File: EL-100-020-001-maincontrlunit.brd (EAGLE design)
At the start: 68 x 86 mm, 13 parts, among them T1 WS-TST-90°, U19 ABS10-32.768KHZ-7-T, U8 MCP7940N-I/SN, U9 PMEG2005ET, X1 944-12-46-00, X2 944-12-46-00

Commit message: update layout
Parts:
- moved X2 0.40 mm to (52.2, 18.5)
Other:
- board size 68 x 86 mm -> 68 x 87 mm
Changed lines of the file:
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@@
 <setting verticaltext="up"/>
 </settings>
-<grid distance="1" unitdist="mm" unit="mm" style="lines" multiple="1" display="no" altdistance="0.025" altunitdist="inch" altunit="inch"/>
+<grid distance="0.1" unitdist="mm" unit="mm" style="lines" multiple="1" display="no" altdistance="0.025" altunitdist="inch" altunit="inch"/>
 <layers>
 <layer number="1" name="Top" color="4" fill="1" visible="yes" active="yes"/>
-<layer number="2" name="Route2" color="1" fill="3" visible="no" active="yes"/>
+<layer number="2" name="Route2" color="1" fill="3" visible="yes" active="yes"/>
 <layer number="3" name="Route3" color="4" fill="3" visible="no" active="no"/>
 <layer number="14" name="Route14" color="1" fill="6" visible="no" active="no"/>
-<layer number="15" name="Route15" color="4" fill="6" visible="no" active="yes"/>
+<layer number="15" name="Route15" color="4" fill="6" visible="yes" active="yes"/>
 <layer number="16" name="Bottom" color="1" fill="1" visible="yes" active="yes"/>
 <layer number="17" name="Pads" color="2" fill="1" visible="yes" active="yes"/>
@@
 <layer number="45" name="Holes" color="7" fill="1" visible="no" active="yes"/>
 <layer number="46" name="Milling" color="3" fill="1" visible="no" active="yes"/>
-<layer number="47" name="Measures" color="7" fill="1" visible="no" active="yes"/>
+<layer number="47" name="Measures" color="7" fill="1" visible="yes" active="yes"/>
 <layer number="48" name="Document" color="7" fill="1" visible="yes" active="yes"/>
 <layer number="49" name="Reference" color="7" fill="1" visible="yes" active="yes"/>
@@
 <plain>
 <wire x1="0" y1="0" x2="68" y2="0" width="0" layer="20"/>
-<wire x1="68" y1="0" x2="68" y2="86" width="0" layer="20"/>
-<wire x1="68" y1="86" x2="0" y2="86" width="0" layer="20"/>
-<wire x1="0" y1="86" x2="0" y2="0" width="0" layer="20"/>
+<wire x1="68" y1="0" x2="68" y2="87" width="0" layer="20"/>
+<wire x1="68" y1="87" x2="0" y2="87" width="0" layer="20"/>
+<wire x1="0" y1="87" x2="0" y2="0" width="0" layer="20"/>
+<dimension x1="3.9" y1="18.54" x2="52.2" y2="18.54" x3="28.05" y3="11" textsize="1.778" layer="47"/>
+<dimension x1="56" y1="52.8" x2="68" y2="52.8" x3="62" y3="49.6" textsize="1.778" layer="47"/>
 </plain>
 <attributes>
@@
 <attribute name="OC_FARNELL" value="unknown" x="3.9" y="18.54" size="1.778" layer="27" rot="R90" display="off"/>
 </element>
-<element name="X2" library="strasys_standard" package="2,54_STIFTLEIST_2X23" value="944-12-46-00" x="52.6" y="18.54" rot="R90">
-<attribute name="MPN" value="" x="52.6" y="18.54" size="1.778" layer="27" rot="R90" display="off"/>
-<attribute name="SUPPLIER" value="W+P" x="52.6" y="18.54" size="1.778" layer="27" rot="R90" display="off"/>
-<attribute name="MF" value="" x="52.6" y="18.54" size="1.778" layer="27" rot="R90" display="off"/>
-<attribute name="OC_FARNELL" value="unknown" x="52.6" y="18.54" size="1.778" layer="27" rot="R90" display="off"/>
+<element name="X2" library="strasys_standard" package="2,54_STIFTLEIST_2X23" value="944-12-46-00" x="52.2" y="18.54" rot="R90">
+<attribute name="MPN" value="" x="52.2" y="18.54" size="1.778" layer="27" rot="R90" display="off"/>
+<attribute name="SUPPLIER" value="W+P" x="52.2" y="18.54" size="1.778" layer="27" rot="R90" display="off"/>
+<attribute name="MF" value="" x="52.2" y="18.54" size="1.778" layer="27" rot="R90" display="off"/>
+<attribute name="OC_FARNELL" value="unknown" x="52.2" y="18.54" size="1.778" layer="27" rot="R90" display="off"/>
 </element>
 </elements>
@@
 <contactref element="X2" pad="P3"/>
 <contactref element="X2" pad="P4"/>
-<wire x1="52.6" y1="21.08" x2="24.8138" y2="59.235" width="0" layer="19" extent="1-1"/>
-<wire x1="55.14" y1="21.08" x2="52.6" y2="21.08" width="0" layer="19" extent="1-1"/>
-<wire x1="37.4782" y1="37.74" x2="52.6" y2="21.08" width="0" layer="19" extent="1-1"/>
+<wire x1="52.2" y1="21.08" x2="24.8138" y2="59.235" width="0" layer="19" extent="1-1"/>
+<wire x1="54.74" y1="21.08" x2="52.2" y2="21.08" width="0" layer="19" extent="1-1"/>
+<wire x1="37.4782" y1="37.74" x2="52.2" y2="21.08" width="0" layer="19" extent="1-1"/>
 <wire x1="24.9512" y1="19.96" x2="37.4782" y2="37.74" width="0" layer="19" extent="1-1"/>
 </signal>
@@
 <contactref element="X2" pad="P44"/>
 <contactref element="X2" pad="P46"/>
-<wire x1="55.14" y1="74.42" x2="36.43" y2="78.84" width="0" layer="19" extent="1-1"/>
-<wire x1="52.6" y1="74.42" x2="55.14" y2="74.42" width="0" layer="19" extent="1-1"/>
-<wire x1="55.14" y1="71.88" x2="55.14" y2="74.42" width="0" layer="19" extent="1-1"/>
-<wire x1="52.6" y1="71.88" x2="52.6" y2="74.42" width="0" layer="19" extent="1-1"/>
-<wire x1="19.8862" y1="55.425" x2="52.6" y2="71.88" width="0" layer="19" extent="1-1"/>
+<wire x1="54.74" y1="74.42" x2="36.43" y2="78.84" width="0" layer="19" extent="1-1"/>
+<wire x1="52.2" y1="74.42" x2="54.74" y2="74.42" width="0" layer="19" extent="1-1"/>
+<wire x1="54.74" y1="71.88" x2="54.74" y2="74.42" width="0" layer="19" extent="1-1"/>
+<wire x1="52.2" y1="71.88" x2="52.2" y2="74.42" width="0" layer="19" extent="1-1"/>
+<wire x1="19.8862" y1="55.425" x2="52.2" y2="71.88" width="0" layer="19" extent="1-1"/>
 <wire x1="6.44" y1="18.54" x2="19.8862" y2="55.425" width="0" layer="19" extent="1-1"/>
 <wire x1="3.9" y1="18.54" x2="6.44" y2="18.54" width="0" layer="19" extent="1-1"/>
-<wire x1="52.6" y1="18.54" x2="6.44" y2="18.54" width="0" layer="19" extent="1-1"/>
-<wire x1="55.14" y1="18.54" x2="52.6" y2="18.54" width="0" layer="19" extent="1-1"/>
-<wire x1="54.56" y1="3.57" x2="55.14" y2="18.54" width="0" layer="19" extent="1-1"/>
+<wire x1="52.2" y1="18.54" x2="6.44" y2="18.54" width="0" layer="19" extent="1-1"/>
+<wire x1="54.74" y1="18.54" x2="52.2" y2="18.54" width="0" layer="19" extent="1-1"/>
+<wire x1="54.56" y1="3.57" x2="54.74" y2="18.54" width="0" layer="19" extent="1-1"/>
 <wire x1="28.3888" y1="28.85" x2="54.56" y2="3.57" width="0" layer="19" extent="1-1"/>
 <wire x1="40.8488" y1="20.96" x2="28.3888" y2="28.85" width="0" layer="19" extent="1-1"/>
@@
 <contactref element="U8" pad="5"/>
 <contactref element="X2" pad="P18"/>
-<wire x1="24.8138" y1="55.425" x2="55.14" y2="38.86" width="0" layer="19" extent="1-1"/>
+<wire x1="24.8138" y1="55.425" x2="54.74" y2="38.86" width="0" layer="19" extent="1-1"/>
 </signal>
 <signal name="I2C1_SCL">
 <contactref element="U8" pad="6"/>
 <contactref element="X2" pad="P17"/>
-<wire x1="24.8138" y1="56.695" x2="52.6" y2="38.86" width="0" layer="19" extent="1-1"/>
+<wire x1="24.8138" y1="56.695" x2="52.2" y2="38.86" width="0" layer="19" extent="1-1"/>
 </signal>
 <signal name="SYS_RESET">
 <contactref element="T1" pad="2"/>
 <contactref element="X2" pad="P10"/>
-<wire x1="50.06" y1="3.57" x2="55.14" y2="28.7" width="0" layer="19" extent="1-1"/>
+<wire x1="50.06" y1="3.57" x2="54.74" y2="28.7" width="0" layer="19" extent="1-1"/>
 </signal>
 <signal name="PE">
@@
 <contactref element="X2" pad="P6"/>
 <contactref element="X2" pad="P5"/>
-<wire x1="52.6" y1="23.62" x2="55.14" y2="23.62" width="0" layer="19" extent="1-1"/>
+<wire x1="52.2" y1="23.62" x2="54.74" y2="23.62" width="0" layer="19" extent="1-1"/>
 </signal>
 <signal name="SYS5V">
 <contactref element="X2" pad="P7"/>
 <contactref element="X2" pad="P8"/>
-<wire x1="52.6" y1="26.16" x2="55.14" y2="26.16" width="0" layer="19" extent="1-1"/>
+<wire x1="52.2" y1="26.16" x2="54.74" y2="26.16" width="0" layer="19" extent="1-1"/>
 </signal>
 <signal name="PWR_BUT">

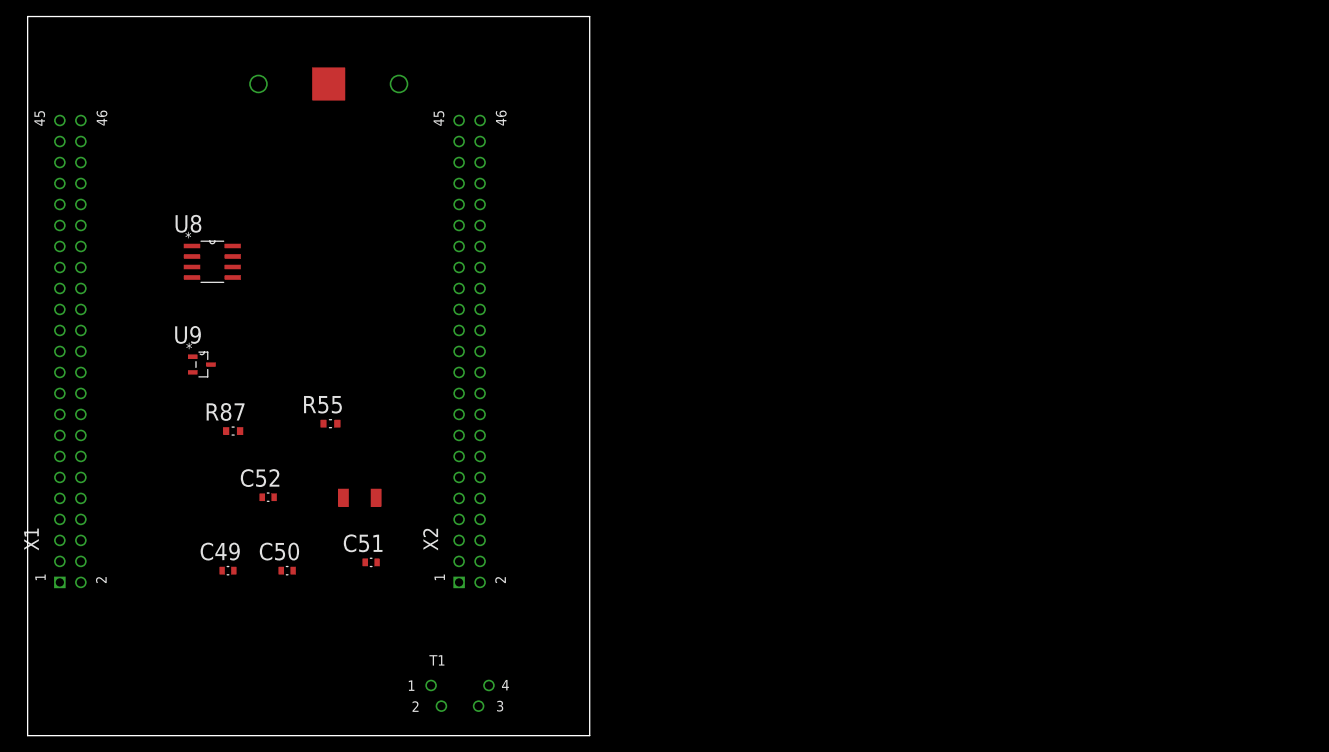
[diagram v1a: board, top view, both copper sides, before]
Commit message: change to size 9
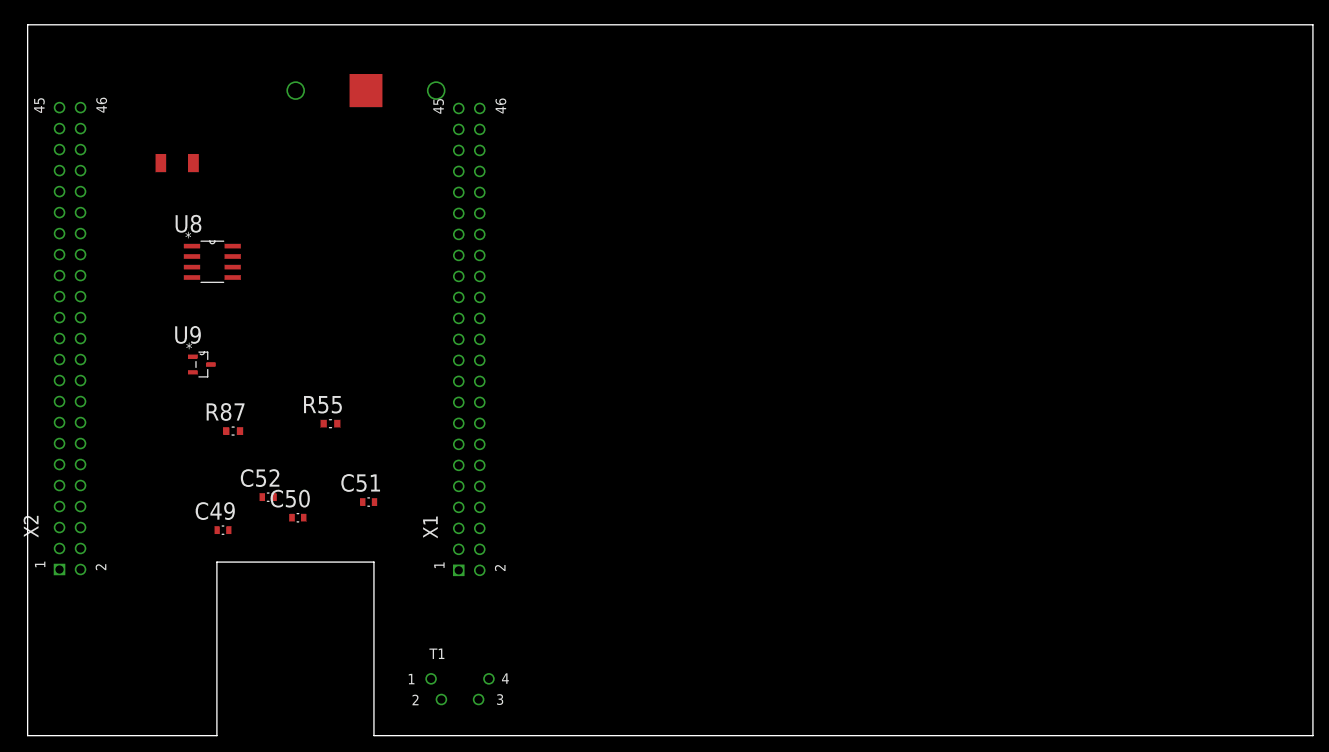
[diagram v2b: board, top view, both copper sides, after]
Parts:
- moved X2 48.4 mm to (3.86, 20.1)
- moved X1 48.3 mm to (52.2, 20.0)
- moved U19 46.1 mm to (18.1, 69.3)
- moved C51 7.31 mm to (41.3, 28.3)
- moved C50 6.53 mm to (32.7, 26.4)
- moved C49 4.94 mm to (23.6, 24.9)
- moved BAT1 4.57 mm to (40.9, 78.0)
- moved T1 0.80 mm to (48.8, 6.87)
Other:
- board size 68 x 87 mm -> 155.5 x 86 mm

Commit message: DIN - Rail
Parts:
- removed R55: 10K Ohms, Vishay_By_element14_Batch_1:RESC1608X60N
- added C1: 47µF, strasys_standard:CAPAE830X650N
- added C10, C3, C4, C5, C6, C7, C8, C9: 10nF, Kemet_By_element14_1:CAPC2013X88N
- added C2, C48: 100nF, Kemet_By_element14_1:CAPC2013X110N
- added D5: SM15T39A, strasys_standard:SM15T39A
- added OC1, OC2, OC3, OC4, OC5, OC6, OC7, OC8: TCMT1106, strasys_standard:SOP-4
- added R1, R2, R3, R4, R5, R6, R7, R8: 1K Ohms, Vishay_By_element14_Batch_1:RESC2013X65N
- added R10, R11, R12, R13, R14, R15, R16, R17: 47K Ohms, Vishay_By_element14_Batch_1:RESC2013X65N
- added R83, R84: 10K Ohms, Vishay_By_element14_Batch_1:RESC2013X65N
- added S1: (no value), switch-dil:SD4-01
- added U1, U2: VNI4140K-32, strasys_standard:SOP80P1030X247-25N
- added U16: 24AA256-I/SN, Microchip_By_element14_Batch_1:SOIC127P600X175-8N
- added X3: 90G-14, strasys_standard:90G-14
- C49: value 0.1uF -> 100nF; device Kemet_By_element14_Batch_1:CAPC1608X85N -> Kemet_By_element14_1:CAPC2013X110N
- C50, C51, C52: device Kemet_By_element14_Batch_1:CAPC1608X85N -> Kemet_By_element14_1:CAPC2013X88N
- R87: device Vishay_By_element14_Batch_1:RESC1608X60N -> Vishay_By_element14_Batch_1:RESC2013X65N
- moved X2 58.5 mm to (62.3, 19.7)
- moved T1 46.3 mm to (2.54, 7.62)
- moved C49 39.3 mm to (41.9, 59.7), turned to 180 degrees
- moved X1 38.1 mm to (14.1, 19.7)
- moved U9 33.8 mm to (50.8, 61.0), turned to 270 degrees
- moved U19 33.6 mm to (43.2, 47.0)
- moved C52 32.9 mm to (49.5, 54.6), turned to 180 degrees
- moved R87 31.9 mm to (49.5, 57.1)
- moved C50 26.6 mm to (45.7, 49.5), turned to 180 degrees
- moved C51 21.3 mm to (40.6, 49.5)
- moved U8 21.0 mm to (43.2, 54.6), turned to 90 degrees
- moved BAT1 6.09 mm to (47.0, 77.5)
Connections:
- net N$35 renamed BAT-SUPPLY
- new net +24V: C1.1, C2.2, D5.K, OC1.4, OC2.4, OC3.4, OC4.4, OC5.4, OC6.4, OC7.4, OC8.4, U1.1, U1.25, U2.1, U2.25
- new net 0V: C1.2, C10.1, C2.1, C3.1, C4.1, C5.1, C6.1, C7.1, C8.1, C9.1, D5.A, R10.2, R11.2, R12.2, R13.2, R14.2, R15.2, R16.2, R17.2, U1.6, U2.6
- new net 24AA_WP: R83.2, S1.1, U16.7
- new net N$14: OC1.1, R1.2
- new net N$15: OC2.1, R2.2
- new net N$16: OC3.1, R3.2
- new net N$17: OC4.1, R4.2
- new net N$19: OC1.3, R10.1, U1.2
- new net N$20: OC2.3, R11.1, U1.4
- new net N$21: OC3.3, R12.1, U1.8
- new net N$22: OC4.3, R13.1, U1.10
- new net N$23: OC5.1, R5.2
- new net N$24: OC6.1, R6.2
- new net N$25: OC7.1, R7.2
- new net N$26: OC8.1, R8.2
- new net N$27: OC5.3, R14.1, U2.2
- new net N$28: OC6.3, R15.1, U2.4
- new net N$29: OC7.3, R16.1, U2.8
- new net N$30: OC8.3, R17.1, U2.10
- new net N$5: R84.2, U16.3
- new net OUT_1: C3.2, U1.22, U1.23, U1.24, X3.1
- new net OUT_10: X3.10
- new net OUT_11: X3.11
- new net OUT_12: X3.12
- new net OUT_2: C4.2, U1.19, U1.20, U1.21, X3.2
- new net OUT_3: C5.2, U1.16, U1.17, U1.18, X3.3
- new net OUT_4: C6.2, U1.13, U1.14, U1.15, X3.4
- new net OUT_5: C7.2, U2.22, U2.23, U2.24, X3.5
- new net OUT_6: C8.2, U2.19, U2.20, U2.21, X3.6
- new net OUT_7: C9.2, U2.16, U2.17, U2.18, X3.7
- new net OUT_8: C10.2, U2.13, U2.14, U2.15, X3.8
- new net OUT_9: X3.9
- net +3.3V: now also C48.2, R83.1, R84.1, U16.8, X1.P3, X1.P4; no longer R55.2, X2.P3, X2.P4
- net AGND: now also X1.P34; no longer X2.P34
- net AIN0: now also X1.P39; no longer X2.P39
- net AIN1: now also X1.P40; no longer X2.P40
- net AIN2: now also X1.P37; no longer X2.P37
- net AIN3: now also X1.P38; no longer X2.P38
- net AIN4: now also X1.P33; no longer X2.P33
- net AIN5: now also X1.P36; no longer X2.P36
- net AIN6: now also X1.P35; no longer X2.P35
- net DGND: now also C48.1, OC1.2, OC2.2, OC3.2, OC4.2, OC5.2, OC6.2, OC7.2, OC8.2, S1.2, U16.1, U16.2, U16.4, X1.P43, X1.P44, X1.P45, X1.P46; no longer X2.P43, X2.P44, X2.P45, X2.P46
- net I2C1_SCL: now also X1.P17; no longer X2.P17
- net I2C1_SDA: now also X1.P18; no longer X2.P18
- net I2C2_SCL: now also U16.6, X1.P19; no longer X2.P19
- net I2C2_SDA: now also U16.5, X1.P20; no longer X2.P20
- net P8_07: now also R1.1, X2.P7; no longer X1.P7
- net P8_08: now also R2.1, X2.P8; no longer X1.P8
- net P8_09: now also R3.1, X2.P9; no longer X1.P9
- net P8_10: now also R4.1, X2.P10; no longer X1.P10
- net P8_11: now also R5.1, X2.P11; no longer X1.P11
- net P8_12: now also R6.1, X2.P12; no longer X1.P12
- net P8_13: now also R7.1, X2.P13; no longer X1.P13
- net P8_14: now also R8.1, X2.P14; no longer X1.P14
- net P8_15: now also X2.P15; no longer X1.P15
- net P8_16: now also X2.P16; no longer X1.P16
- net P8_17: now also X2.P17; no longer X1.P17
- net P8_18: now also X2.P18; no longer X1.P18
- net P8_19: now also X2.P19; no longer R55.1, U8.7, X1.P19
- net P8_26: now also X2.P26; no longer X1.P26
- net P9_12: now also X1.P12; no longer X2.P12
- net P9_14: now also X1.P14; no longer X2.P14
- net P9_15: now also X1.P15; no longer X2.P15
- net P9_16: now also X1.P16; no longer X2.P16
- net P9_23: now also X1.P23; no longer X2.P23
- net P9_27: now also X1.P27; no longer X2.P27
- net P9_30: now also X1.P30; no longer X2.P30
- net P9_41: now also X1.P41; no longer X2.P41
- net P9_42: now also X1.P42; no longer X2.P42
- net PWR_BUT: now also X1.P9; no longer X2.P9
- net SYS5V: now also X1.P7, X1.P8; no longer X2.P7, X2.P8
- net SYS_RESET: now also X1.P10; no longer X2.P10
- net UART1_RXD: now also X1.P26; no longer X2.P26
- net UART1_TXD: now also X1.P24; no longer X2.P24
- net UART2_RXD: now also X1.P22; no longer X2.P22
- net UART2_TXD: now also X1.P21; no longer X2.P21
- net UART4_RXD: now also X1.P11; no longer X2.P11
- net UART4_TXD: now also X1.P13; no longer X2.P13
- net VADC_1.8V: now also X1.P32; no longer X2.P32
- net VDD5V: now also X1.P5, X1.P6; no longer X2.P5, X2.P6
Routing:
- net BAT-SUPPLY: track 0.00 -> 35.6 mm, vias 0 -> 1
- net DGND: track 0.00 -> 20.4 mm, vias 0 -> 6
- net N$47: track 0.00 -> 9.08 mm
- net N$48: track 0.00 -> 7.02 mm
- net N$51: track 0.00 -> 5.33 mm
- net N$46: track 0.00 -> 2.85 mm
- net +3.3V: track 0.00 -> 2.69 mm
- added copper zone on layer 2, net DGND
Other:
- board size 155.5 x 86 mm -> 155.6 x 86 mm
- board text added: "5V DC"
- board text added: "Ethernet"
- board text added: "USB"
